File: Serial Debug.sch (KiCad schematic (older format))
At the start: 19 parts, among them J7 USB_OTG, U9 FT230XQ

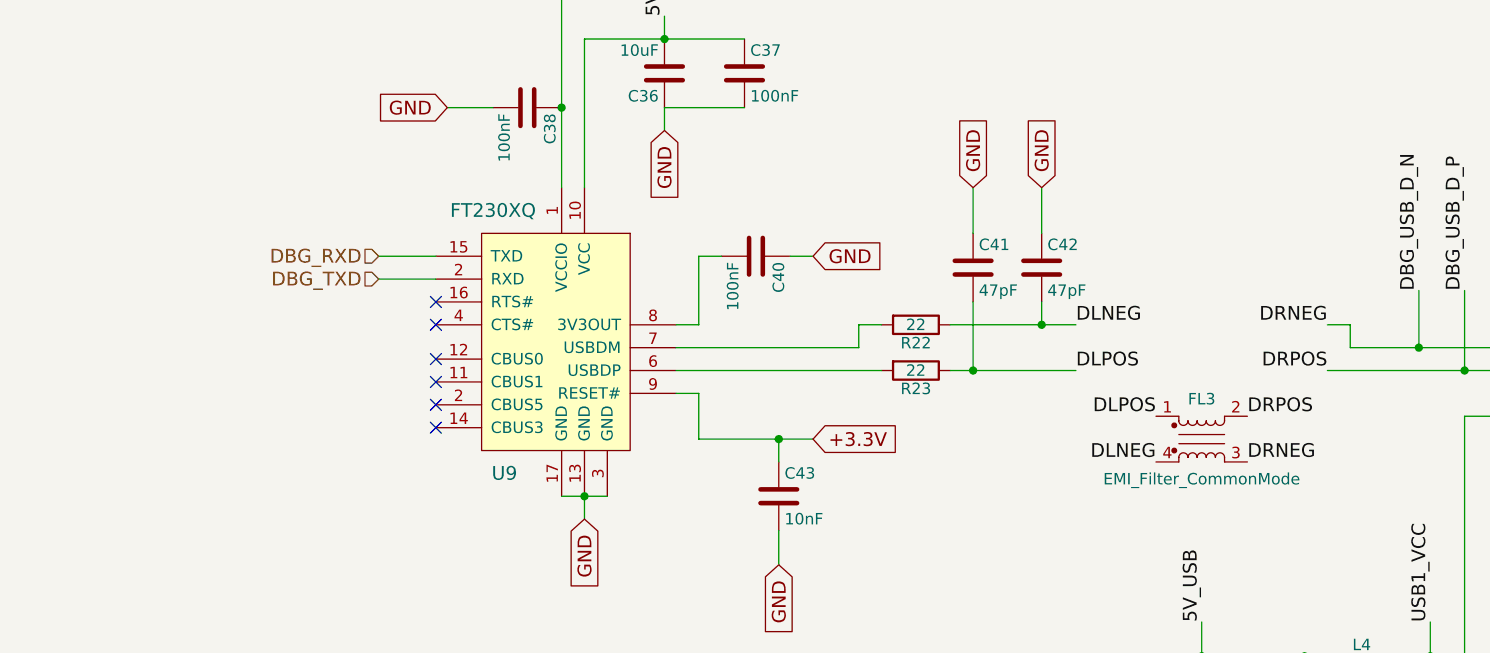
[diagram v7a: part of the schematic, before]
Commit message: almost completely routed; few missing routes
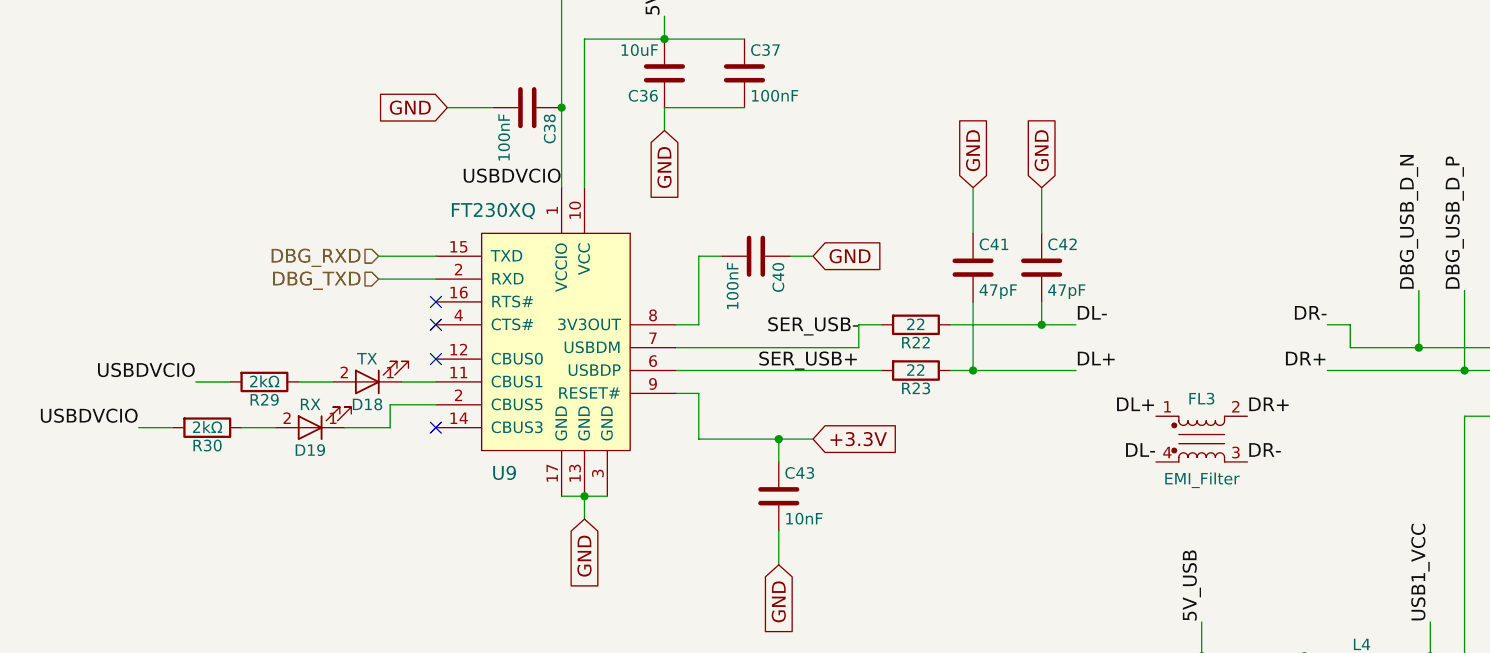
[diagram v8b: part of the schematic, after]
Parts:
- added D18: TX, LEDs:LED_1206, symbol LED
- added D19: RX, LEDs:LED_1206, symbol LED
- added R29, R30: 2kΩ, Resistors_SMD:R_0603_HandSoldering, symbol R
- FL3: value EMI_Filter_CommonMode -> EMI_Filter
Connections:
- net +3.3V: now also R29.2, R30.2
- net at U9.11 (CBUS1): now also D18.1 (K)
- net SER_USB+: now reaches R23.2, U9.6 (USBDP)
- net SER_USB-: now reaches R22.2, U9.7 (USBDM)
- net DLNEG renamed DL-
- net DLPOS renamed DL+
- new net: D19.1 (K), U9.2 (RXD)
- new net: D19.2 (A), R30.1
- new net: D18.2 (A), R29.1
- no-connect marks 7 -> 5
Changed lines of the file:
@@
 EESchema Schematic File Version 2
 LIBS:viztisztito-rescue
-LIBS:power
-LIBS:device
-LIBS:transistors
-LIBS:conn
-LIBS:linear
-LIBS:regul
-LIBS:74xx
-LIBS:cmos4000
-LIBS:adc-dac
-LIBS:memory
-LIBS:xilinx
-LIBS:microcontrollers
-LIBS:dsp
-LIBS:microchip
-LIBS:analog_switches
-LIBS:motorola
-LIBS:texas
-LIBS:intel
-LIBS:audio
-LIBS:interface
-LIBS:digital-audio
-LIBS:philips
-LIBS:display
-LIBS:cypress
-LIBS:siliconi
-LIBS:opto
-LIBS:atmel
-LIBS:contrib
-LIBS:valves
-LIBS:analog_devices
 LIBS:vtx-214-015-112
 LIBS:viztisztito-cache
@@
 LIBS:RFSolutions
 LIBS:switches
-EELAYER 25 0
+LIBS:74xgxx
+LIBS:74xx
+LIBS:ac-dc
+LIBS:actel
+LIBS:adc-dac
+LIBS:allegro
+LIBS:Altera
+LIBS:analog_devices
+LIBS:analog_switches
+LIBS:atmel
+LIBS:audio
+LIBS:battery_management
+LIBS:bbd
+LIBS:bosch
+LIBS:brooktre
+LIBS:cmos4000
+LIBS:conn
+LIBS:contrib
+LIBS:cypress
+LIBS:device
+LIBS:digital-audio
+LIBS:diode
+LIBS:display
+LIBS:dsp
+LIBS:elec-unifil
+LIBS:ESD_Protection
+LIBS:ftdi
+LIBS:gennum
+LIBS:graphic_symbols
+LIBS:hc11
+LIBS:infineon
+LIBS:intel
+LIBS:interface
+LIBS:intersil
+LIBS:ir
+LIBS:Lattice
+LIBS:leds
+LIBS:LEM
+LIBS:linear
+LIBS:logic_programmable
+LIBS:maxim
+LIBS:mechanical
+LIBS:memory
+LIBS:microchip
+LIBS:microchip_dspic33dsc
+LIBS:microchip_pic10mcu
+LIBS:microchip_pic12mcu
+LIBS:microchip_pic16mcu
+LIBS:microchip_pic18mcu
+LIBS:microchip_pic24mcu
+LIBS:microchip_pic32mcu
+LIBS:microcontrollers
+LIBS:modules
+LIBS:motor_drivers
+LIBS:motorola
+LIBS:motors
+LIBS:msp430
+LIBS:nordicsemi
+LIBS:nxp
+LIBS:nxp_armmcu
+LIBS:onsemi
+LIBS:opto
+LIBS:Oscillators
+LIBS:philips
+LIBS:power
+LIBS:powerint
+LIBS:Power_Management
+LIBS:pspice
+LIBS:references
+LIBS:regul
+LIBS:relays
+LIBS:rfcom
+LIBS:sensors
+LIBS:silabs
+LIBS:siliconi
+LIBS:stm8
+LIBS:stm32
+LIBS:supertex
+LIBS:texas
+LIBS:transf
+LIBS:transistors
+LIBS:triac_thyristor
+LIBS:ttl_ieee
+LIBS:valves
+LIBS:video
+LIBS:wiznet
+LIBS:Worldsemi
+LIBS:Xicor
+LIBS:xilinx
+LIBS:Zilog
+LIBS:crystals_oscillators
+LIBS:Diodes
+LIBS:discrete_transistors
+LIBS:microcontrollers_dspic33dsc
+LIBS:microcontrollers_msp430
+LIBS:microcontrollers_pic10mcu
+LIBS:microcontrollers_pic12mcu
+LIBS:microcontrollers_pic16mcu
+LIBS:microcontrollers_pic18mcu
+LIBS:microcontrollers_pic32mcu
+LIBS:microcontrollers_stm8
+LIBS:microcontrollers_stm32
+LIBS:microcontrollers_xmc
+LIBS:misc
+LIBS:Passives
+LIBS:regulators
+LIBS:rf
+EELAYER 26 0
 EELAYER END
 $Descr A4 11693 8268
@@
 GND
 NoConn ~ 2050 3600
-NoConn ~ 2050 3500
-NoConn ~ 2050 3400
 NoConn ~ 2050 3300
 NoConn ~ 2050 3150
@@
 P 5400 3650
 F 0 "FL3" H 5400 3825 50  0000 C CNN
-F 1 "EMI_Filter_CommonMode" H 5400 3475 50  0000 C CNN
+F 1 "EMI_Filter" H 5400 3475 50  0000 C CNN
 F 2 "water:744233121" V 5400 3690 50  0001 C CNN
 F 3 "http://hu.farnell.com/wurth-elektronik/744233121/line-filter-lvds-0805-120ohm-0/dp/1848957" V 5400 3690 50  0001 C CNN
@@
 	4300 3350 4850 3350
 Text Label 5600 3550 0    60   ~ 0
-DRPOS
+DR+
 Text Label 5600 3750 0    60   ~ 0
-DRNEG
+DR-
 Text Label 5200 3550 2    60   ~ 0
-DLPOS
+DL+
 Text Label 5200 3750 2    60   ~ 0
-DLNEG
+DL-
 Text Label 5950 3150 2    60   ~ 0
-DRNEG
+DR-
 Text Label 5950 3350 2    60   ~ 0
-DRPOS
+DR+
 Text Label 4850 3350 0    60   ~ 0
-DLPOS
+DL+
 Text Label 4850 3150 0    60   ~ 0
-DLNEG
+DL-
+Text Label 3900 3200 2    60   ~ 0
+SER_USB-
+Text Label 3900 3350 2    60   ~ 0
+SER_USB+
+Wire Wire Line
+	750  3600 900  3600
+Wire Wire Line
+	1200 3600 1350 3600
+Wire Wire Line
+	1650 3600 1850 3600
+$Comp
+L R R30
+U 1 1 59ADB2E3
+P 1050 3600
+F 0 "R30" V 1130 3600 50  0000 C CNN
+F 1 "2kΩ" V 1050 3600 50  0000 C CNN
+F 2 "Resistors_SMD:R_0603_HandSoldering" V 980 3600 50  0001 C CNN
+F 3 "hu.farnell.com/multicomp/mcwr06x2001ftl/res-thick-film-2k-1-0-1w-0603/dp/2447319" H 1050 3600 50  0001 C CNN
+	1    1050 3600
+	0    1    1    0
+$EndComp
+$Comp
+L LED D19
+U 1 1 59ADB2EA
+P 1500 3600
+F 0 "D19" H 1500 3700 50  0000 C CNN
+F 1 "RX" H 1500 3500 50  0000 C CNN
+F 2 "LEDs:LED_1206" H 1500 3600 50  0001 C CNN
+F 3 "http://hu.farnell.com/lumex/sml-lx1206gw-tr/led-2mm-x-1-6mm-green-10mcd-565nm/dp/2062262" H 1500 3600 50  0001 C CNN
+	1    1500 3600
+	-1   0    0    1
+$EndComp
+Wire Wire Line
+	1000 3400 1150 3400
+Wire Wire Line
+	1450 3400 1600 3400
+Wire Wire Line
+	1900 3400 2050 3400
+$Comp
+L R R29
+U 1 1 59ADB910
+P 1300 3400
+F 0 "R29" V 1380 3400 50  0000 C CNN
+F 1 "2kΩ" V 1300 3400 50  0000 C CNN
+F 2 "Resistors_SMD:R_0603_HandSoldering" V 1230 3400 50  0001 C CNN
+F 3 "hu.farnell.com/multicomp/mcwr06x2001ftl/res-thick-film-2k-1-0-1w-0603/dp/2447319" H 1300 3400 50  0001 C CNN
+	1    1300 3400
+	0    1    1    0
+$EndComp
+$Comp
+L LED D18
+U 1 1 59ADB916
+P 1750 3400
+F 0 "D18" H 1750 3500 50  0000 C CNN
+F 1 "TX" H 1750 3300 50  0000 C CNN
+F 2 "LEDs:LED_1206" H 1750 3400 50  0001 C CNN
+F 3 "http://hu.farnell.com/lumex/sml-lx1206gw-tr/led-2mm-x-1-6mm-green-10mcd-565nm/dp/2062262" H 1750 3400 50  0001 C CNN
+	1    1750 3400
+	-1   0    0    1
+$EndComp
+Wire Wire Line
+	1850 3600 1850 3500
+Wire Wire Line
+	1850 3500 2050 3500
+Text Label 2600 2550 2    60   ~ 0
+USBDVCIO
+Text Label 1000 3400 2    60   ~ 0
+USBDVCIO
+Text Label 750  3600 2    60   ~ 0
+USBDVCIO
 $EndSCHEMATC
